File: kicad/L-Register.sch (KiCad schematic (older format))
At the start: 19 parts, among them U128 74LS245, U129 74LS173, U130 74LS173

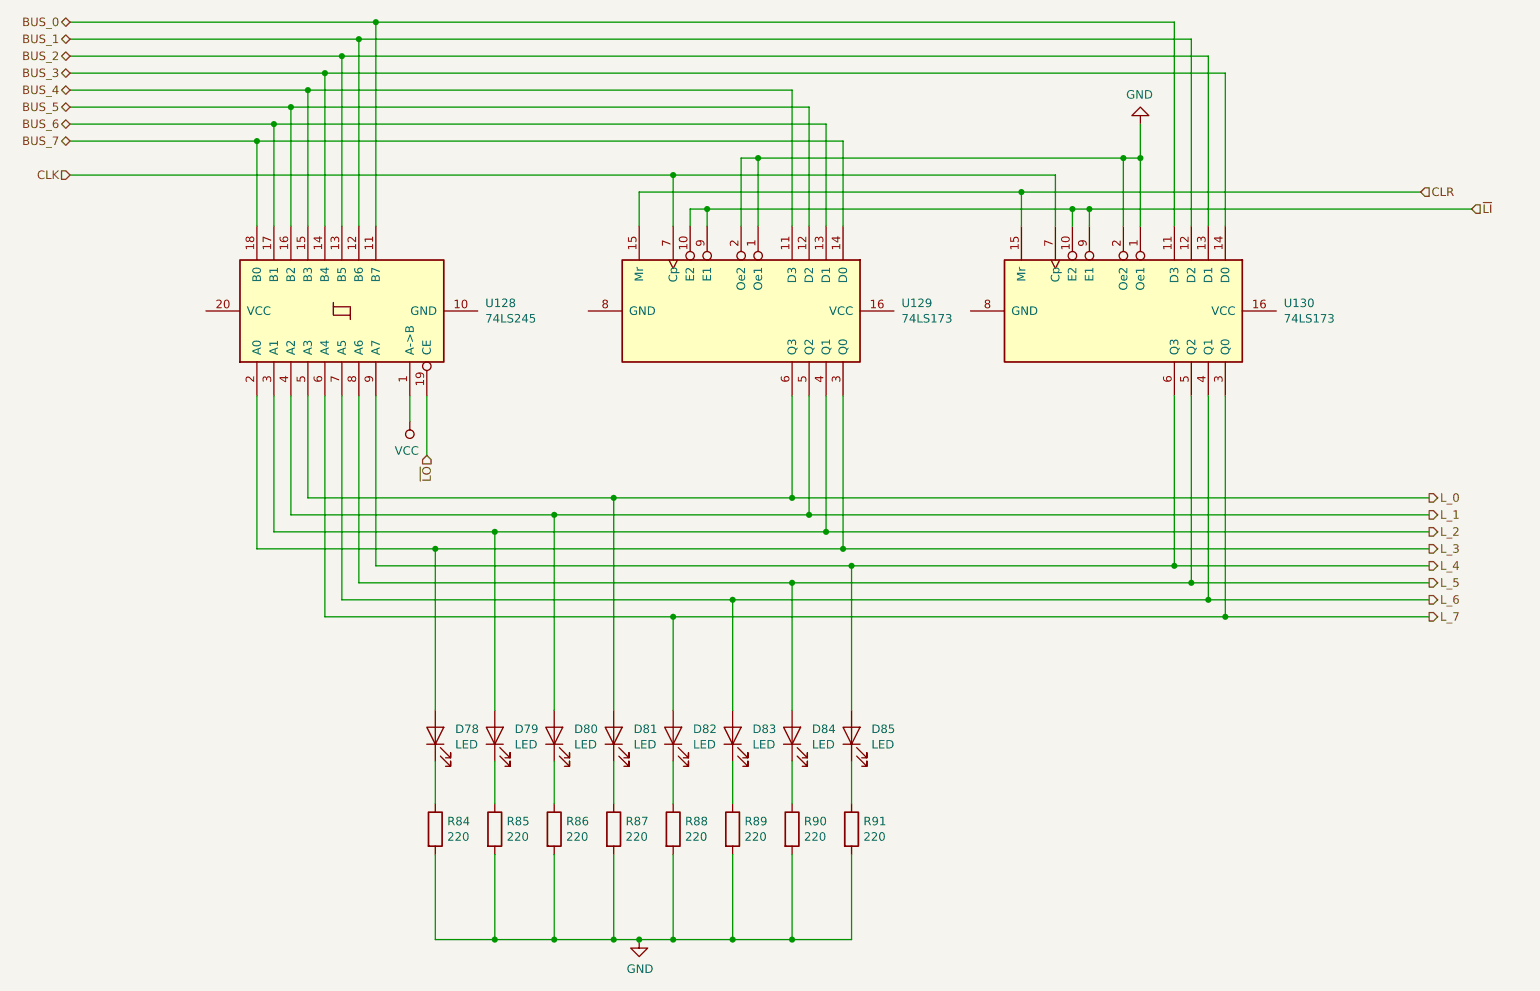
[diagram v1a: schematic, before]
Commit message: Reorganize part references
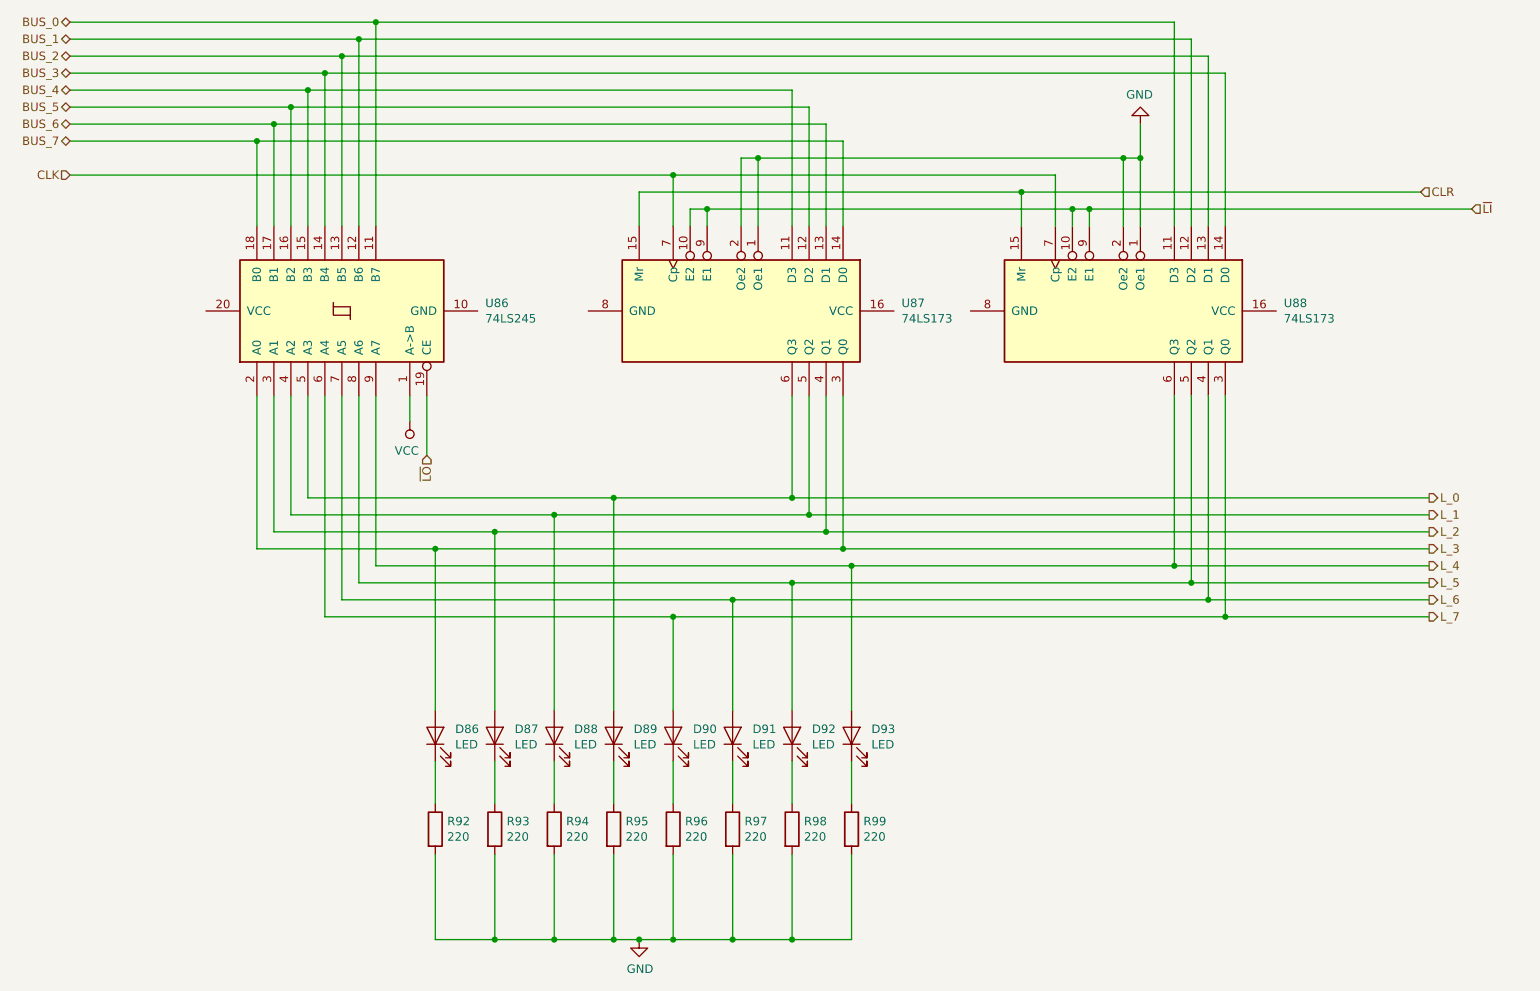
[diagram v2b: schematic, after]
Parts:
- renumbered D78 to D86, D79 to D87, D80 to D88, D81 to D89, D82 to D90, D83 to D91, D84 to D92, D85 to D93, R84 to R92, R85 to R93, R86 to R94, R87 to R95, R88 to R96, R89 to R97, R90 to R98, R91 to R99, U128 to U86, U129 to U87, U130 to U88
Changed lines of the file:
@@
 $Descr USLetter 11000 8500
 encoding utf-8
-Sheet 8 26
+Sheet 24 26
 Title "L Register"
 Date "2019-10-03"
@@
 AR Path="/5D9C73BD/5DA803F5" Ref="U?"  Part="1"
 AR Path="/5D9E8F35/5DA803F5" Ref="U?"  Part="1"
-AR Path="/5DA98D6D/5DA9A5C9/5DA803F5" Ref="U128"  Part="1"
-F 0 "U128" V 2896 2456 50  0000 R CNN
+AR Path="/5DA98D6D/5DA9A5C9/5DA803F5" Ref="U86"  Part="1"
+F 0 "U86" V 2896 2456 50  0000 R CNN
 F 1 "74LS245" V 2805 2456 50  0000 R CNN
 F 2 "" H 2850 3300 50  0001 C CNN
@@
 AR Path="/5D9C73BD/5DA80422" Ref="U?"  Part="1"
 AR Path="/5D9E8F35/5DA80422" Ref="U?"  Part="1"
-AR Path="/5DA98D6D/5DA9A5C9/5DA80422" Ref="U130"  Part="1"
-F 0 "U130" V 7404 4244 50  0000 L CNN
+AR Path="/5DA98D6D/5DA9A5C9/5DA80422" Ref="U88"  Part="1"
+F 0 "U88" V 7404 4244 50  0000 L CNN
 F 1 "74LS173" V 7495 4244 50  0000 L CNN
 F 2 "" H 7450 3300 50  0001 C CNN
@@
 AR Path="/5D9C73BD/5DA8044C" Ref="D?"  Part="1"
 AR Path="/5D9E8F35/5DA8044C" Ref="D?"  Part="1"
-AR Path="/5DA98D6D/5DA9A5C9/5DA8044C" Ref="D78"  Part="1"
-F 0 "D78" V 3439 5683 50  0000 R CNN
+AR Path="/5DA98D6D/5DA9A5C9/5DA8044C" Ref="D86"  Part="1"
+F 0 "D86" V 3439 5683 50  0000 R CNN
 F 1 "LED" V 3348 5683 50  0000 R CNN
 F 2 "" H 3400 5800 50  0001 C CNN
@@
 AR Path="/5D9C73BD/5DA80452" Ref="D?"  Part="1"
 AR Path="/5D9E8F35/5DA80452" Ref="D?"  Part="1"
-AR Path="/5DA98D6D/5DA9A5C9/5DA80452" Ref="D79"  Part="1"
-F 0 "D79" V 3789 5683 50  0000 R CNN
+AR Path="/5DA98D6D/5DA9A5C9/5DA80452" Ref="D87"  Part="1"
+F 0 "D87" V 3789 5683 50  0000 R CNN
 F 1 "LED" V 3698 5683 50  0000 R CNN
 F 2 "" H 3750 5800 50  0001 C CNN
@@
 AR Path="/5D9C73BD/5DA80458" Ref="D?"  Part="1"
 AR Path="/5D9E8F35/5DA80458" Ref="D?"  Part="1"
-AR Path="/5DA98D6D/5DA9A5C9/5DA80458" Ref="D80"  Part="1"
-F 0 "D80" V 4139 5683 50  0000 R CNN
+AR Path="/5DA98D6D/5DA9A5C9/5DA80458" Ref="D88"  Part="1"
+F 0 "D88" V 4139 5683 50  0000 R CNN
 F 1 "LED" V 4048 5683 50  0000 R CNN
 F 2 "" H 4100 5800 50  0001 C CNN
@@
 AR Path="/5D9C73BD/5DA8045E" Ref="D?"  Part="1"
 AR Path="/5D9E8F35/5DA8045E" Ref="D?"  Part="1"
-AR Path="/5DA98D6D/5DA9A5C9/5DA8045E" Ref="D81"  Part="1"
-F 0 "D81" V 4489 5683 50  0000 R CNN
+AR Path="/5DA98D6D/5DA9A5C9/5DA8045E" Ref="D89"  Part="1"
+F 0 "D89" V 4489 5683 50  0000 R CNN
 F 1 "LED" V 4398 5683 50  0000 R CNN
 F 2 "" H 4450 5800 50  0001 C CNN
@@
 AR Path="/5D9C73BD/5DA80464" Ref="D?"  Part="1"
 AR Path="/5D9E8F35/5DA80464" Ref="D?"  Part="1"
-AR Path="/5DA98D6D/5DA9A5C9/5DA80464" Ref="D82"  Part="1"
-F 0 "D82" V 4839 5683 50  0000 R CNN
+AR Path="/5DA98D6D/5DA9A5C9/5DA80464" Ref="D90"  Part="1"
+F 0 "D90" V 4839 5683 50  0000 R CNN
 F 1 "LED" V 4748 5683 50  0000 R CNN
 F 2 "" H 4800 5800 50  0001 C CNN
@@
 AR Path="/5D9C73BD/5DA8046A" Ref="D?"  Part="1"
 AR Path="/5D9E8F35/5DA8046A" Ref="D?"  Part="1"
-AR Path="/5DA98D6D/5DA9A5C9/5DA8046A" Ref="D83"  Part="1"
-F 0 "D83" V 5189 5683 50  0000 R CNN
+AR Path="/5DA98D6D/5DA9A5C9/5DA8046A" Ref="D91"  Part="1"
+F 0 "D91" V 5189 5683 50  0000 R CNN
 F 1 "LED" V 5098 5683 50  0000 R CNN
 F 2 "" H 5150 5800 50  0001 C CNN
@@
 AR Path="/5D9C73BD/5DA80470" Ref="D?"  Part="1"
 AR Path="/5D9E8F35/5DA80470" Ref="D?"  Part="1"
-AR Path="/5DA98D6D/5DA9A5C9/5DA80470" Ref="D84"  Part="1"
-F 0 "D84" V 5539 5683 50  0000 R CNN
+AR Path="/5DA98D6D/5DA9A5C9/5DA80470" Ref="D92"  Part="1"
+F 0 "D92" V 5539 5683 50  0000 R CNN
 F 1 "LED" V 5448 5683 50  0000 R CNN
 F 2 "" H 5500 5800 50  0001 C CNN
@@
 AR Path="/5D9C73BD/5DA80476" Ref="D?"  Part="1"
 AR Path="/5D9E8F35/5DA80476" Ref="D?"  Part="1"
-AR Path="/5DA98D6D/5DA9A5C9/5DA80476" Ref="D85"  Part="1"
-F 0 "D85" V 5889 5683 50  0000 R CNN
+AR Path="/5DA98D6D/5DA9A5C9/5DA80476" Ref="D93"  Part="1"
+F 0 "D93" V 5889 5683 50  0000 R CNN
 F 1 "LED" V 5798 5683 50  0000 R CNN
 F 2 "" H 5850 5800 50  0001 C CNN
@@
 AR Path="/5D9C73BD/5DA80492" Ref="R?"  Part="1"
 AR Path="/5D9E8F35/5DA80492" Ref="R?"  Part="1"
-AR Path="/5DA98D6D/5DA9A5C9/5DA80492" Ref="R84"  Part="1"
-F 0 "R84" H 3470 6396 50  0000 L CNN
+AR Path="/5DA98D6D/5DA9A5C9/5DA80492" Ref="R92"  Part="1"
+F 0 "R92" H 3470 6396 50  0000 L CNN
 F 1 "220" H 3470 6305 50  0000 L CNN
 F 2 "" V 3330 6350 50  0001 C CNN
@@
 AR Path="/5D9C73BD/5DA80498" Ref="R?"  Part="1"
 AR Path="/5D9E8F35/5DA80498" Ref="R?"  Part="1"
-AR Path="/5DA98D6D/5DA9A5C9/5DA80498" Ref="R85"  Part="1"
-F 0 "R85" H 3820 6396 50  0000 L CNN
+AR Path="/5DA98D6D/5DA9A5C9/5DA80498" Ref="R93"  Part="1"
+F 0 "R93" H 3820 6396 50  0000 L CNN
 F 1 "220" H 3820 6305 50  0000 L CNN
 F 2 "" V 3680 6350 50  0001 C CNN
@@
 AR Path="/5D9C73BD/5DA8049E" Ref="R?"  Part="1"
 AR Path="/5D9E8F35/5DA8049E" Ref="R?"  Part="1"
-AR Path="/5DA98D6D/5DA9A5C9/5DA8049E" Ref="R86"  Part="1"
-F 0 "R86" H 4170 6396 50  0000 L CNN
+AR Path="/5DA98D6D/5DA9A5C9/5DA8049E" Ref="R94"  Part="1"
+F 0 "R94" H 4170 6396 50  0000 L CNN
 F 1 "220" H 4170 6305 50  0000 L CNN
 F 2 "" V 4030 6350 50  0001 C CNN
@@
 AR Path="/5D9C73BD/5DA804A4" Ref="R?"  Part="1"
 AR Path="/5D9E8F35/5DA804A4" Ref="R?"  Part="1"
-AR Path="/5DA98D6D/5DA9A5C9/5DA804A4" Ref="R87"  Part="1"
-F 0 "R87" H 4520 6396 50  0000 L CNN
+AR Path="/5DA98D6D/5DA9A5C9/5DA804A4" Ref="R95"  Part="1"
+F 0 "R95" H 4520 6396 50  0000 L CNN
 F 1 "220" H 4520 6305 50  0000 L CNN
 F 2 "" V 4380 6350 50  0001 C CNN
@@
 AR Path="/5D9C73BD/5DA804AA" Ref="R?"  Part="1"
 AR Path="/5D9E8F35/5DA804AA" Ref="R?"  Part="1"
-AR Path="/5DA98D6D/5DA9A5C9/5DA804AA" Ref="R88"  Part="1"
-F 0 "R88" H 4870 6396 50  0000 L CNN
+AR Path="/5DA98D6D/5DA9A5C9/5DA804AA" Ref="R96"  Part="1"
+F 0 "R96" H 4870 6396 50  0000 L CNN
 F 1 "220" H 4870 6305 50  0000 L CNN
 F 2 "" V 4730 6350 50  0001 C CNN
@@
 AR Path="/5D9C73BD/5DA804B0" Ref="R?"  Part="1"
 AR Path="/5D9E8F35/5DA804B0" Ref="R?"  Part="1"
-AR Path="/5DA98D6D/5DA9A5C9/5DA804B0" Ref="R89"  Part="1"
-F 0 "R89" H 5220 6396 50  0000 L CNN
+AR Path="/5DA98D6D/5DA9A5C9/5DA804B0" Ref="R97"  Part="1"
+F 0 "R97" H 5220 6396 50  0000 L CNN
 F 1 "220" H 5220 6305 50  0000 L CNN
 F 2 "" V 5080 6350 50  0001 C CNN
@@
 AR Path="/5D9C73BD/5DA804B6" Ref="R?"  Part="1"
 AR Path="/5D9E8F35/5DA804B6" Ref="R?"  Part="1"
-AR Path="/5DA98D6D/5DA9A5C9/5DA804B6" Ref="R90"  Part="1"
-F 0 "R90" H 5570 6396 50  0000 L CNN
+AR Path="/5DA98D6D/5DA9A5C9/5DA804B6" Ref="R98"  Part="1"
+F 0 "R98" H 5570 6396 50  0000 L CNN
 F 1 "220" H 5570 6305 50  0000 L CNN
 F 2 "" V 5430 6350 50  0001 C CNN
@@
 AR Path="/5D9C73BD/5DA804BC" Ref="R?"  Part="1"
 AR Path="/5D9E8F35/5DA804BC" Ref="R?"  Part="1"
-AR Path="/5DA98D6D/5DA9A5C9/5DA804BC" Ref="R91"  Part="1"
-F 0 "R91" H 5920 6396 50  0000 L CNN
+AR Path="/5DA98D6D/5DA9A5C9/5DA804BC" Ref="R99"  Part="1"
+F 0 "R99" H 5920 6396 50  0000 L CNN
 F 1 "220" H 5920 6305 50  0000 L CNN
 F 2 "" V 5780 6350 50  0001 C CNN
@@
 AR Path="/5D9C73BD/5DA8050D" Ref="U?"  Part="1"
 AR Path="/5D9E8F35/5DA8050D" Ref="U?"  Part="1"
-AR Path="/5DA98D6D/5DA9A5C9/5DA8050D" Ref="U129"  Part="1"
-F 0 "U129" V 5154 4244 50  0000 L CNN
+AR Path="/5DA98D6D/5DA9A5C9/5DA8050D" Ref="U87"  Part="1"
+F 0 "U87" V 5154 4244 50  0000 L CNN
 F 1 "74LS173" V 5245 4244 50  0000 L CNN
 F 2 "" H 5200 3300 50  0001 C CNN
